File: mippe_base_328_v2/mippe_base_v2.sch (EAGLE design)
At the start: 22 parts, among them J9 BURNIN, SW1 BTN-PTS810, U1 ATMEGA328P-AUR, Y1 16MHz

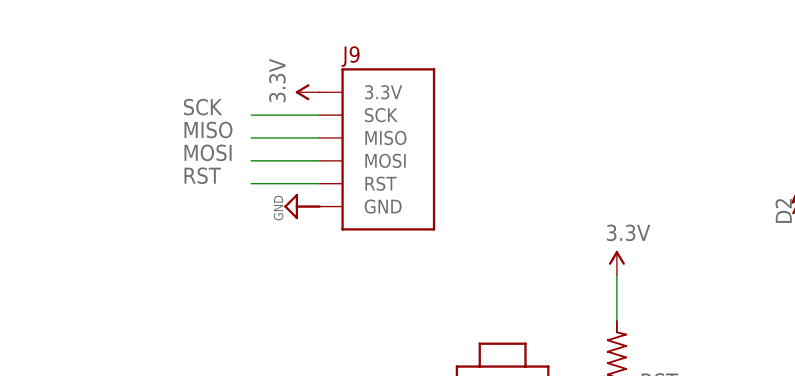
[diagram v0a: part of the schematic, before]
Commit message: update burnin drill size
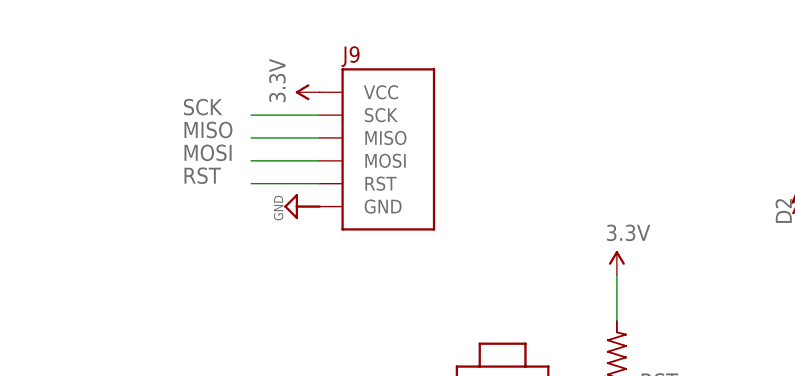
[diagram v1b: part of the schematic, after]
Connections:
- net 3.3V: now also J9.VCC; no longer J9.3.3V
